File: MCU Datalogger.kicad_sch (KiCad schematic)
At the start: 25 parts, among them U1 DS1337S+, U2 24LC1025, U3 24LC1025, U4 ATMEGA328P-AU, Y1 32.768 KHz, Y2 16 MHz

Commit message: Using PWR_FLAG symbols to suppress to errors.
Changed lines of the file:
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@@
 	)
 	(junction
+		(at 66.04 135.89)
+		(diameter 0)
+		(color 0 0 0 0)
+	)
+	(junction
 		(at 99.06 36.83)
 		(diameter 0)
@@
 	)
 	(junction
+		(at 77.47 111.76)
+		(diameter 0)
+		(color 0 0 0 0)
+	)
+	(junction
 		(at 243.84 74.93)
 		(diameter 0)
@@
 	(wire
 		(pts
+			(xy 77.47 111.76) (xy 77.47 115.57)
+		)
+		(stroke
+			(width 0)
+			(type default)
+		)
+	)
+	(wire
+		(pts
 			(xy 209.55 41.91) (xy 217.17 41.91)
 		)
@@
 	(wire
 		(pts
+			(xy 66.04 135.89) (xy 91.44 135.89)
+		)
+		(stroke
+			(width 0)
+			(type default)
+		)
+	)
+	(wire
+		(pts
 			(xy 99.06 36.83) (xy 111.76 36.83)
 		)
@@
 	(wire
 		(pts
-			(xy 77.47 109.22) (xy 77.47 115.57)
+			(xy 41.91 109.22) (xy 41.91 115.57)
 		)
 		(stroke
@@
 	(wire
 		(pts
-			(xy 41.91 109.22) (xy 41.91 115.57)
+			(xy 132.08 49.53) (xy 132.08 59.69)
 		)
 		(stroke
@@
 	(wire
 		(pts
-			(xy 132.08 49.53) (xy 132.08 59.69)
+			(xy 43.18 50.8) (xy 24.13 50.8)
 		)
 		(stroke
@@
 	(wire
 		(pts
-			(xy 43.18 50.8) (xy 24.13 50.8)
+			(xy 63.5 135.89) (xy 66.04 135.89)
+		)
+		(stroke
+			(width 0)
+			(type default)
+		)
+	)
+	(wire
+		(pts
+			(xy 66.04 135.89) (xy 66.04 138.43)
 		)
 		(stroke
@@
 	(wire
 		(pts
+			(xy 74.93 110.49) (xy 74.93 111.76)
+		)
+		(stroke
+			(width 0)
+			(type default)
+		)
+	)
+	(wire
+		(pts
 			(xy 54.61 134.62) (xy 41.91 134.62)
 		)
@@
 	(wire
 		(pts
+			(xy 72.39 110.49) (xy 74.93 110.49)
+		)
+		(stroke
+			(width 0)
+			(type default)
+		)
+	)
+	(wire
+		(pts
 			(xy 157.48 69.85) (xy 157.48 73.66)
 		)
@@
 	(wire
 		(pts
-			(xy 63.5 135.89) (xy 91.44 135.89)
+			(xy 232.41 74.93) (xy 217.17 74.93)
 		)
 		(stroke
@@
 	(wire
 		(pts
-			(xy 232.41 74.93) (xy 217.17 74.93)
+			(xy 138.43 49.53) (xy 132.08 49.53)
 		)
 		(stroke
@@
 	(wire
 		(pts
-			(xy 138.43 49.53) (xy 132.08 49.53)
+			(xy 248.92 41.91) (xy 248.92 44.45)
 		)
 		(stroke
@@
 	(wire
 		(pts
-			(xy 248.92 41.91) (xy 248.92 44.45)
+			(xy 74.93 111.76) (xy 77.47 111.76)
 		)
 		(stroke
@@
 	(wire
 		(pts
+			(xy 77.47 109.22) (xy 77.47 111.76)
+		)
+		(stroke
+			(width 0)
+			(type default)
+		)
+	)
+	(wire
+		(pts
 			(xy 99.06 36.83) (xy 99.06 43.18)
 		)
@@
 	)
 	(symbol
+		(lib_id "power:PWR_FLAG")
+		(at 72.39 110.49 90)
+		(unit 1)
+		(exclude_from_sim no)
+		(in_bom yes)
+		(on_board yes)
+		(dnp no)
+		(fields_autoplaced yes)
+		(property "Reference" "#FLG03"
+			(at 70.485 110.49 0)
+			(effects
+				(font
+					(size 1.27 1.27)
+				)
+				(hide yes)
+			)
+		)
+		(property "Value" "PWR_FLAG"
+			(at 68.58 110.4899 90)
+			(effects
+				(font
+					(size 1.27 1.27)
+				)
+				(justify left)
+			)
+		)
+		(property "Footprint" ""
+			(at 72.39 110.49 0)
+			(effects
+				(font
+					(size 1.27 1.27)
+				)
+				(hide yes)
+			)
+		)
+		(property "Datasheet" "~"
+			(at 72.39 110.49 0)
+			(effects
+				(font
+					(size 1.27 1.27)
+				)
+				(hide yes)
+			)
+		)
+		(property "Description" "Special symbol for telling ERC where power comes from"
+			(at 72.39 110.49 0)
+			(effects
+				(font
+					(size 1.27 1.27)
+				)
+				(hide yes)
+			)
+		)
+		(pin "1"
+		)
+		(instances
+			(project "MCU Datalogger"
+				(path "/b0e7f133-88ab-429e-b3bf-607c46cef14a"
+					(reference "#FLG03")
+					(unit 1)
+				)
+			)
+		)
+	)
+	(symbol
 		(lib_id "ATMEGA328P-AU:ATMEGA328P-AU")
 		(at 189.23 67.31 0)
@@
 	)
 	(symbol
+		(lib_id "power:PWR_FLAG")
+		(at 66.04 138.43 180)
+		(unit 1)
+		(exclude_from_sim no)
+		(in_bom yes)
+		(on_board yes)
+		(dnp no)
+		(fields_autoplaced yes)
+		(property "Reference" "#FLG04"
+			(at 66.04 140.335 0)
+			(effects
+				(font
+					(size 1.27 1.27)
+				)
+				(hide yes)
+			)
+		)
+		(property "Value" "PWR_FLAG"
+			(at 66.04 143.51 0)
+			(effects
+				(font
+					(size 1.27 1.27)
+				)
+			)
+		)
+		(property "Footprint" ""
+			(at 66.04 138.43 0)
+			(effects
+				(font
+					(size 1.27 1.27)
+				)
+				(hide yes)
+			)
+		)
+		(property "Datasheet" "~"
+			(at 66.04 138.43 0)
+			(effects
+				(font
+					(size 1.27 1.27)
+				)
+				(hide yes)
+			)
+		)
+		(property "Description" "Special symbol for telling ERC where power comes from"
+			(at 66.04 138.43 0)
+			(effects
+				(font
+					(size 1.27 1.27)
+				)
+				(hide yes)
+			)
+		)
+		(pin "1"
+		)
+		(instances
+			(project "MCU Datalogger"
+				(path "/b0e7f133-88ab-429e-b3bf-607c46cef14a"
+					(reference "#FLG04")
+					(unit 1)
+				)
+			)
+		)
+	)
+	(symbol
 		(lib_id "Mechanical:MountingHole")
 		(at 231.14 121.92 0)
@@
 			)
 		)
+		(property "Purpose" ""
+			(at 77.47 123.19 0)
+			(effects
+				(font
+					(size 1.27 1.27)
+				)
+			)
+		)

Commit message: Completed comments.
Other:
- note added: "EEPROM"
- note added: "MCU"
- note added: "Mounting"
- note added: "Real time clock"
- moved on the sheet: H1, H2, H3, H4
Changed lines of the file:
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@@
+		)
+	)
+	(rectangle
+		(start 128.27 26.035)
+		(end 260.985 105.41)
+		(stroke
+			(width 0)
+			(type dot)
+		)
+		(fill
+			(type none)
+		)
+	)
+	(rectangle
+		(start 223.52 110.49)
+		(end 252.095 146.05)
+		(stroke
+			(width 0)
+			(type dot)
+		)
+		(fill
+			(type none)
+		)
+	)
+	(rectangle
+		(start 25.4 102.87)
+		(end 124.46 147.32)
+		(stroke
+			(width 0)
+			(type dot)
+		)
+		(fill
+			(type none)
+		)
+	)
+	(rectangle
+		(start 20.32 26.035)
+		(end 122.555 81.915)
+		(stroke
+			(width 0)
+			(type dot)
+		)
+		(fill
+			(type none)
+		)
+	)
+	(text "Real time clock"
+		(exclude_from_sim no)
+		(at 27.813 24.765 0)
+		(effects
+			(font
+				(size 1.27 1.27)
+			)
+		)
+	)
+	(text "MCU"
+		(exclude_from_sim no)
+		(at 129.921 24.765 0)
+		(effects
+			(font
+				(size 1.27 1.27)
+			)
+		)
+	)
+	(text "Mounting"
+		(exclude_from_sim no)
+		(at 227.457 108.966 0)
+		(effects
+			(font
+				(size 1.27 1.27)
+			)
+		)
+	)
+	(text "EEPROM"
+		(exclude_from_sim no)
+		(at 28.956 101.346 0)
+		(effects
+			(font
+				(size 1.27 1.27)
+			)
 		)
 	)
@@
 	(symbol
 		(lib_id "Mechanical:MountingHole")
-		(at 231.14 121.92 0)
+		(at 231.14 132.08 0)
 		(unit 1)
 		(exclude_from_sim no)
@@
 		(fields_autoplaced yes)
 		(property "Reference" "H3"
-			(at 233.68 120.6499 0)
+			(at 233.68 130.8099 0)
 			(effects
 				(font
@@
 		)
 		(property "Value" "MountingHole"
-			(at 233.68 123.1899 0)
+			(at 233.68 133.3499 0)
 			(effects
 				(font
@@
 		)
 		(property "Footprint" "MountingHole:MountingHole_2.1mm"
-			(at 231.14 121.92 0)
+			(at 231.14 132.08 0)
 			(effects
 				(font
@@
 		)
 		(property "Datasheet" "~"
-			(at 231.14 121.92 0)
+			(at 231.14 132.08 0)
 			(effects
 				(font
@@
 		)
 		(property "Description" "Mounting Hole without connection"
-			(at 231.14 121.92 0)
+			(at 231.14 132.08 0)
 			(effects
 				(font
@@
 	(symbol
 		(lib_id "Mechanical:MountingHole")
-		(at 231.14 106.68 0)
+		(at 231.14 116.84 0)
 		(unit 1)
 		(exclude_from_sim no)
@@
 		(fields_autoplaced yes)
 		(property "Reference" "H1"
-			(at 233.68 105.4099 0)
+			(at 233.68 115.5699 0)
 			(effects
 				(font
@@
 		)
 		(property "Value" "MountingHole"
-			(at 233.68 107.9499 0)
+			(at 233.68 118.1099 0)
 			(effects
 				(font
@@
 		)
 		(property "Footprint" "MountingHole:MountingHole_2.1mm"
-			(at 231.14 106.68 0)
+			(at 231.14 116.84 0)
 			(effects
 				(font
@@
 		)
 		(property "Datasheet" "~"
-			(at 231.14 106.68 0)
+			(at 231.14 116.84 0)
 			(effects
 				(font
@@
 		)
 		(property "Description" "Mounting Hole without connection"
-			(at 231.14 106.68 0)
+			(at 231.14 116.84 0)
 			(effects
 				(font
@@
 	(symbol
 		(lib_id "Mechanical:MountingHole")
-		(at 231.14 114.3 0)
+		(at 231.14 124.46 0)
 		(unit 1)
 		(exclude_from_sim no)
@@
 		(fields_autoplaced yes)
 		(property "Reference" "H2"
-			(at 233.68 113.0299 0)
+			(at 233.68 123.1899 0)
 			(effects
 				(font
@@
 		)
 		(property "Value" "MountingHole"
-			(at 233.68 115.5699 0)
+			(at 233.68 125.7299 0)
 			(effects
 				(font
@@
 		)
 		(property "Footprint" "MountingHole:MountingHole_2.1mm"
-			(at 231.14 114.3 0)
+			(at 231.14 124.46 0)
 			(effects
 				(font
@@
 		)
 		(property "Datasheet" "~"
-			(at 231.14 114.3 0)
+			(at 231.14 124.46 0)
 			(effects
 				(font
@@
 		)
 		(property "Description" "Mounting Hole without connection"
-			(at 231.14 114.3 0)
+			(at 231.14 124.46 0)
 			(effects
 				(font
@@
 	(symbol
 		(lib_id "Mechanical:MountingHole")
-		(at 231.14 128.27 0)
+		(at 231.14 138.43 0)
 		(unit 1)
 		(exclude_from_sim no)
@@
 		(fields_autoplaced yes)
 		(property "Reference" "H4"
-			(at 233.68 126.9999 0)
+			(at 233.68 137.1599 0)
 			(effects
 				(font
@@
 		)
 		(property "Value" "MountingHole"
-			(at 233.68 129.5399 0)
+			(at 233.68 139.6999 0)
 			(effects
 				(font
@@
 		)
 		(property "Footprint" "MountingHole:MountingHole_2.1mm"
-			(at 231.14 128.27 0)
+			(at 231.14 138.43 0)
 			(effects
 				(font
@@
 		)
 		(property "Datasheet" "~"
-			(at 231.14 128.27 0)
+			(at 231.14 138.43 0)
 			(effects
 				(font
@@
 		)
 		(property "Description" "Mounting Hole without connection"
-			(at 231.14 128.27 0)
-			(effects
-				(font
+			(at 231.14 138.43 0)
+			(effects
+				(font

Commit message: Completed wiring. Many improvements pending.
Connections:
- net Vcc: now also BT1.1 (+), C5.1, D2.2 (A), U4.18 (AVCC), U4.4 (VCC)
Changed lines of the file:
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@@
+	)
+	(label "Vcc"
+		(at 245.11 41.91 0)
+		(fields_autoplaced yes)
+		(effects
+			(font
+				(size 1.27 1.27)
+			)
+			(justify left bottom)
+		)
 	)
 	(label "Vcc"

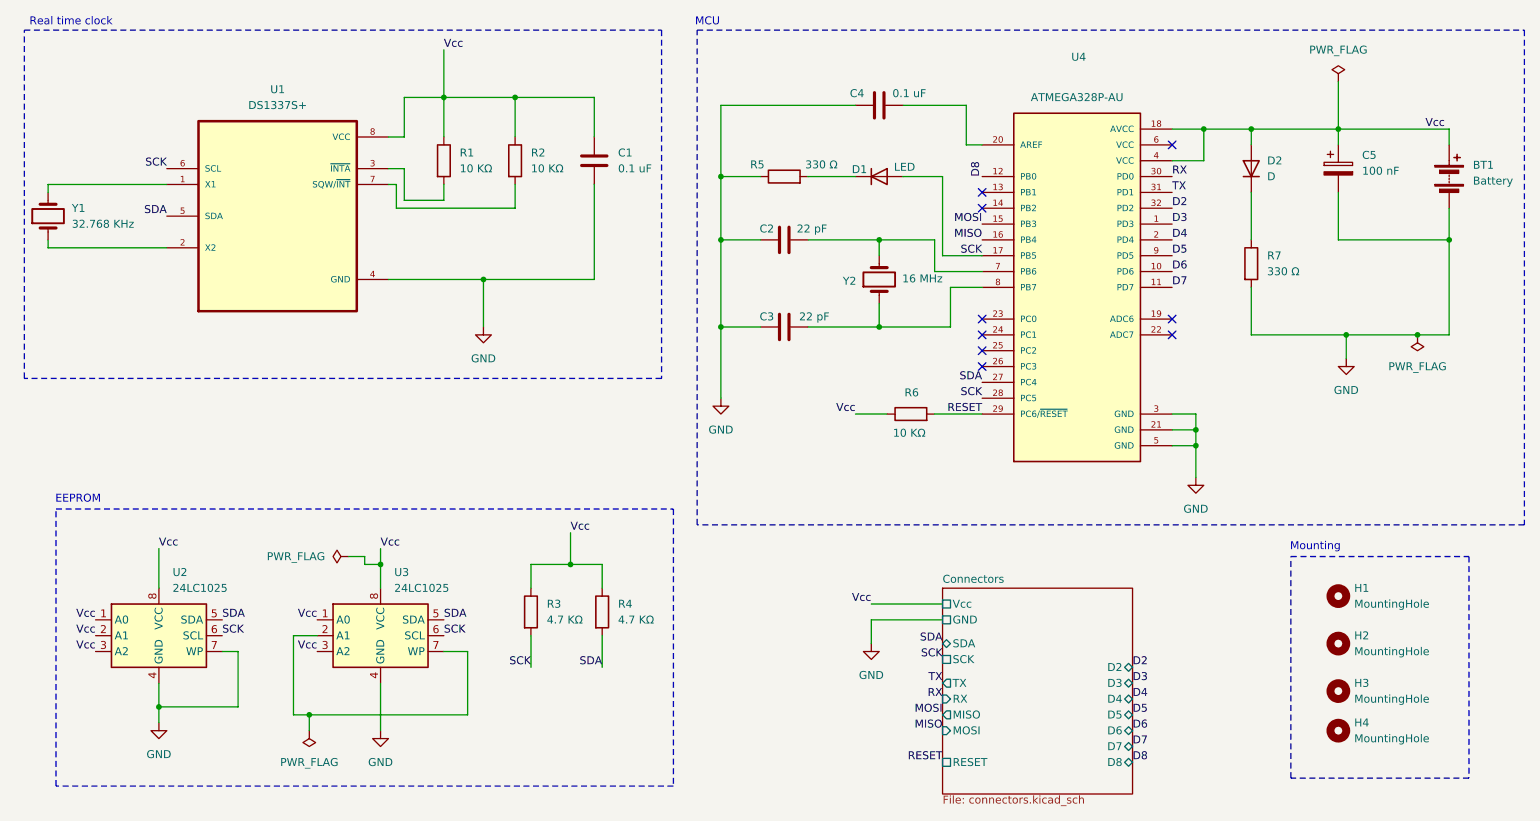
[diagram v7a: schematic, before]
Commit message: Fixed issue with I2C SCL.
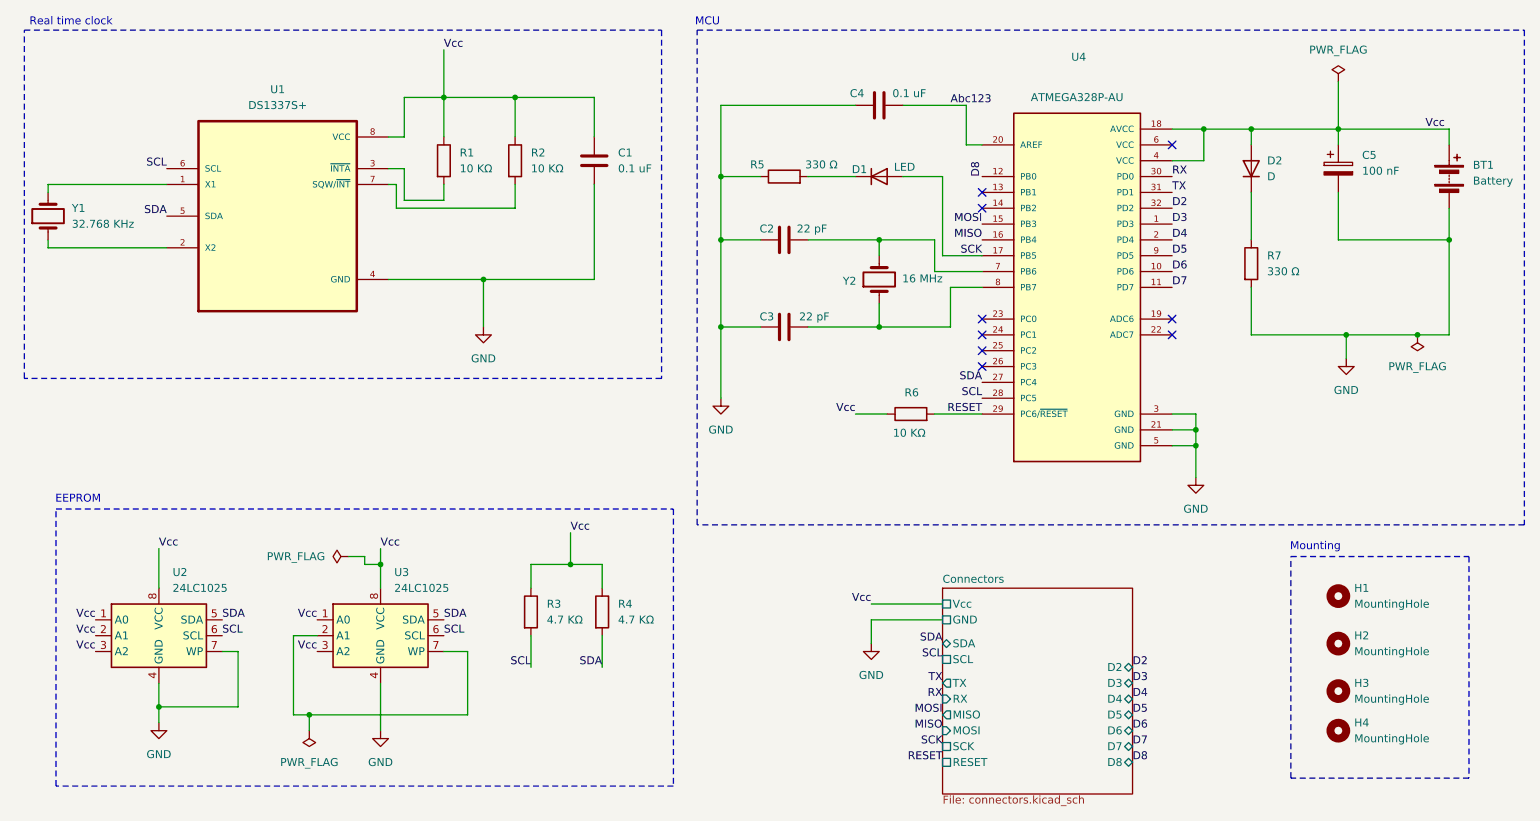
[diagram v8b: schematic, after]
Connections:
- net SCK: no longer R3.2, U1.6 (SCL), U2.6 (SCL), U3.6 (SCL), U4.28 (PC5)
- net Abc123: now reaches C4.2, U4.20 (AREF)
- new net SCL: R3.2, U1.6 (SCL), U2.6 (SCL), U3.6 (SCL), U4.28 (PC5)
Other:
- sheet Connectors ports: added SCL; removed none
